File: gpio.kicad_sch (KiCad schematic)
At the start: 7 parts, among them J1 CONN_02X20, J2 CONN_02X20, J3 hub75-abcd, J5 hub75-abcd, U1 LFE5U-85F-6BG381C

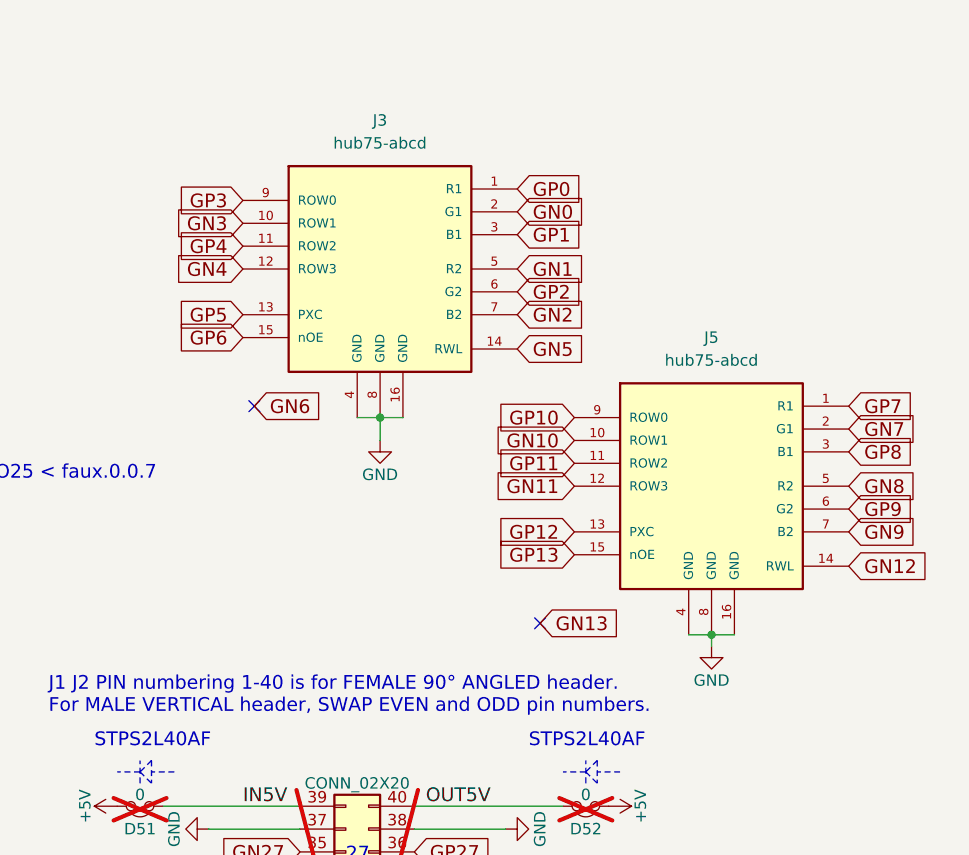
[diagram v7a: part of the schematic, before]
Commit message: update shematic for new hub75 connector
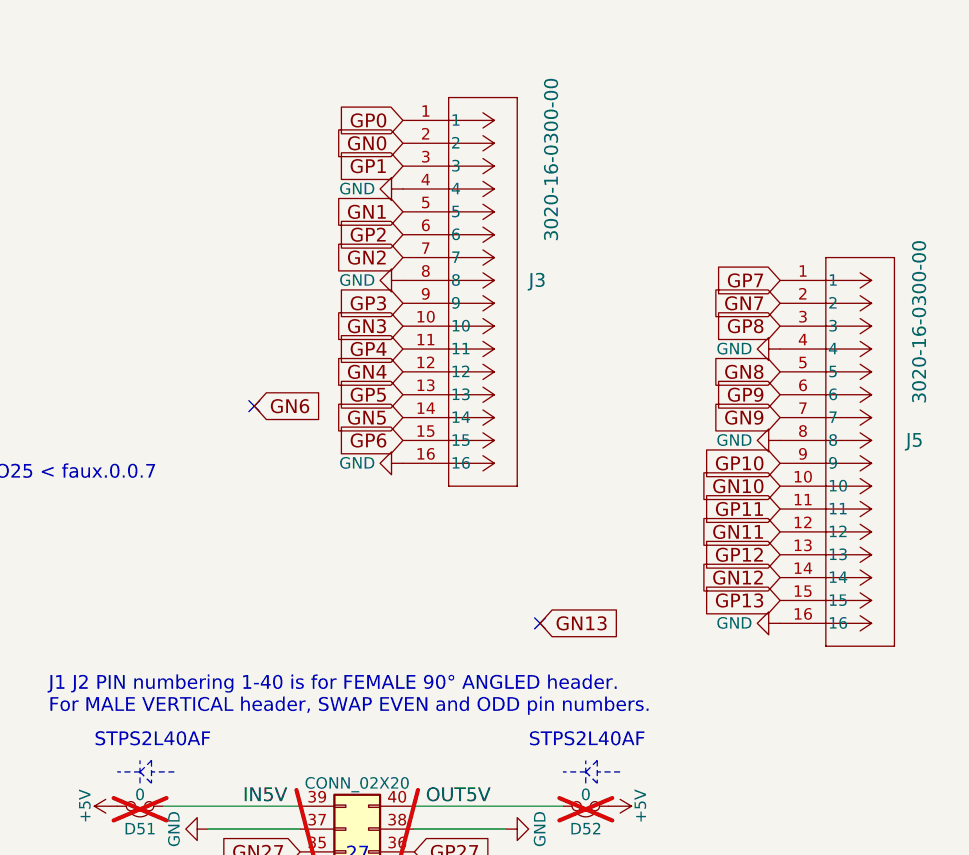
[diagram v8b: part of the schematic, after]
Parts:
- removed J3, J5: hub75-abcd, Socket_Strips:SAMTEC-HTST-108-01-X-DV, symbol samtec:hub75-abcd
- added J3, J5: 3020-16-0300-00, hub75:CONN16_3020-16-0300-00_CNC, symbol hub75:3020-16-0300-00
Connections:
- net GN0: now also J3.2
- net GN1: now also J3.5
- net GN10: now also J5.10
- net GN11: now also J5.12
- net GN12: now also J5.14
- net GN2: now also J3.7
- net GN3: now also J3.10
- net GN4: now also J3.12
- net GN5: now also J3.14
- net GN7: now also J5.2
- net GN8: now also J5.5
- net GN9: now also J5.7
- net GND: now also J3.16, J3.4, J3.8, J5.16, J5.4, J5.8
- net GP0: now also J3.1
- net GP1: now also J3.3
- net GP10: now also J5.9
- net GP11: now also J5.11
- net GP12: now also J5.13
- net GP13: now also J5.15
- net GP2: now also J3.6
- net GP3: now also J3.9
- net GP4: now also J3.11
- net GP5: now also J3.13
- net GP6: now also J3.15
- net GP7: now also J5.1
- net GP8: now also J5.3
- net GP9: now also J5.6
